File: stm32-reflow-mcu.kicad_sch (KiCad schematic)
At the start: 34 parts, among them J1 TC2030, J10 63824-1, J11 63824-1, J12 63824-1, J2 Conn_01x04_Male, J3 Conn_01x03_Male, J4 Screw_Terminal_01x02, J5 Screw_Terminal_01x02, J7 63824-1, J8 63824-1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

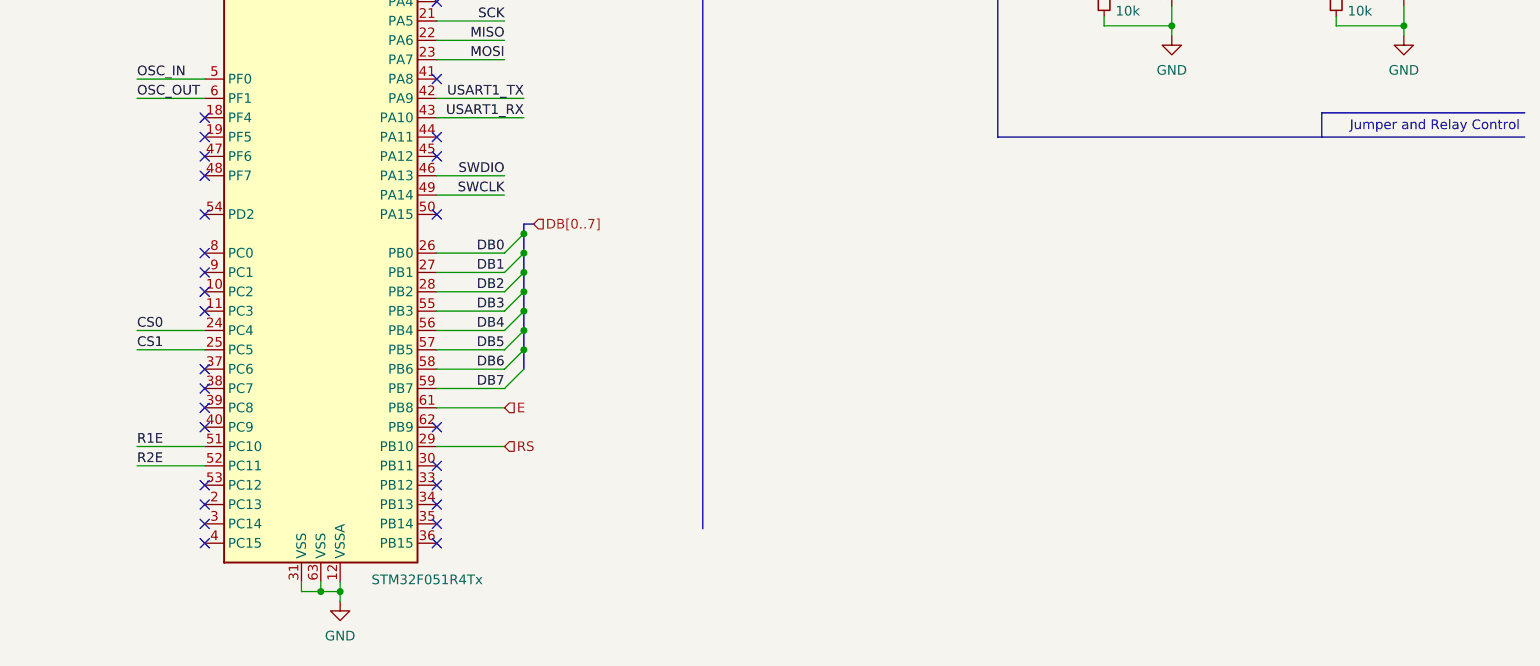
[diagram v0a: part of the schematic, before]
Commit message: added encoder interface
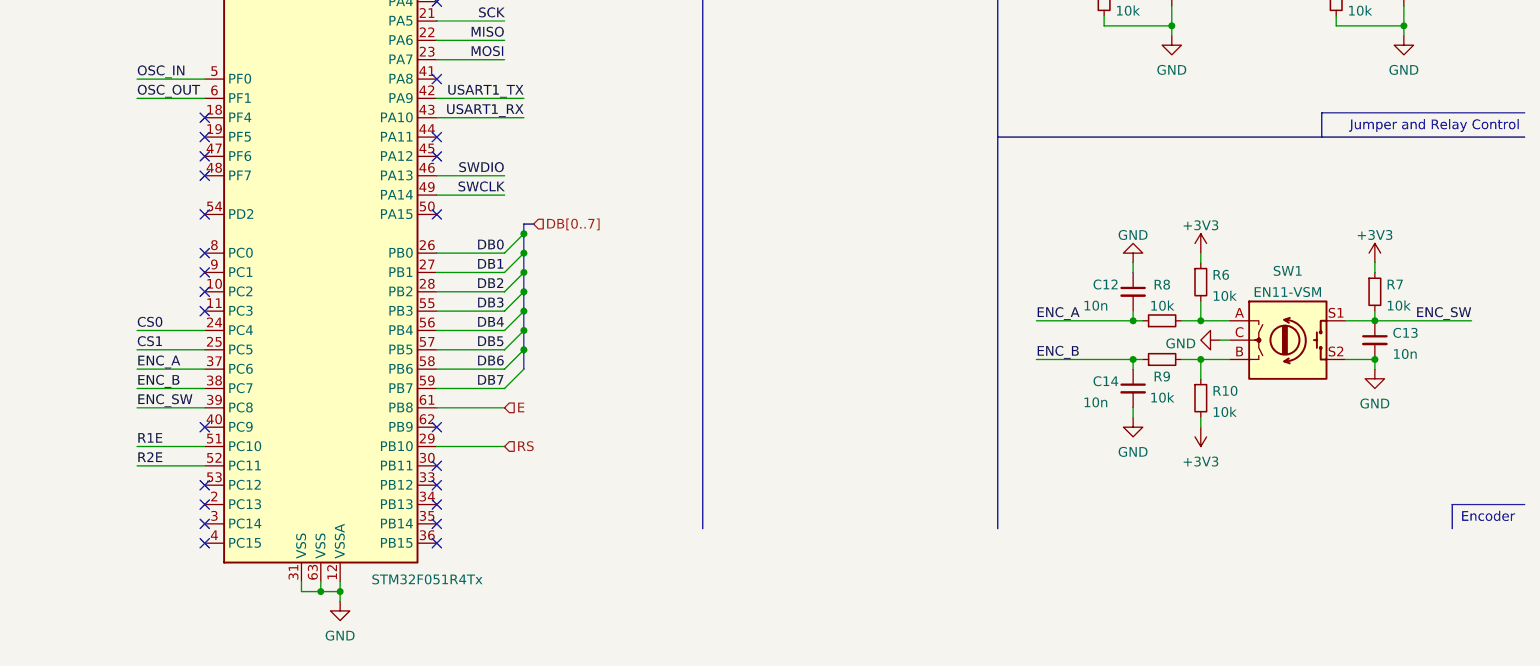
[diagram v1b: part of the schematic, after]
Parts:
- added C12, C13, C14: 10n, Capacitor_SMD:C_0603_1608Metric, symbol Device:C_Small
- added R10, R6, R7, R8, R9: 10k, Resistor_SMD:R_0603_1608Metric, symbol Device:R_Small
- added SW1: EN11-VSM, Personal:EN11-VSM1AF20, symbol Device:Rotary_Encoder_Switch
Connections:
- net +3V3: now also R10.2, R6.1, R7.1
- net GND: now also C12.1, C13.2, C14.2, SW1.C, SW1.S2
- net ENC_A: now reaches U1.37 (PC6)
- net ENC_A: now also C12.2, R8.1
- net ENC_B: now reaches U1.38 (PC7)
- net ENC_B: now also C14.1, R9.1
- net ENC_SW: now reaches U1.39 (PC8)
- net ENC_SW: now also C13.1, R7.2, SW1.S1
- new net: R6.2, R8.2, SW1.A
- new net: R10.1, R9.2, SW1.B
- no-connect marks 33 -> 30
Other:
- note added: "Encoder"

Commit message: added revision label, finalized for fabrication
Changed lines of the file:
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@@
   (title_block
     (title "STM32 Reflow Controller")
-    (date "2021-11-26")
+    (date "2021-11-29")
+    (rev "07684a7")
     (company "de Byl Technologies, LLC")
   )

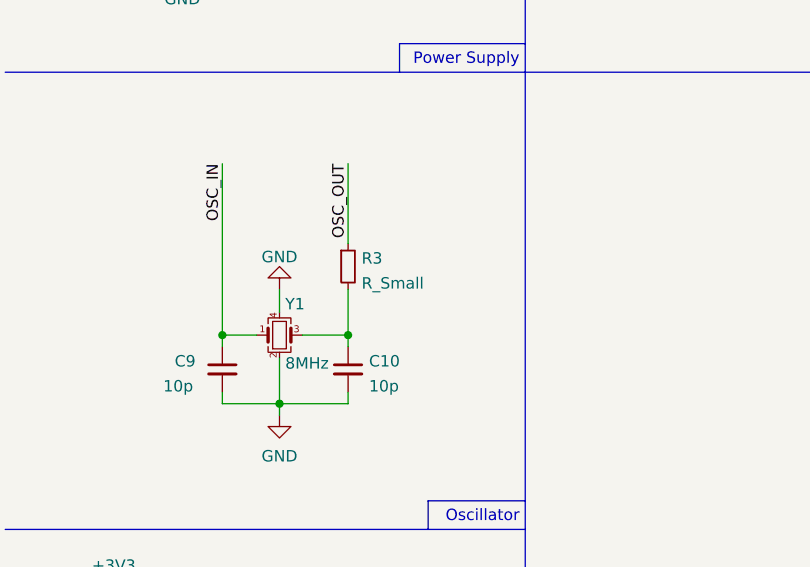
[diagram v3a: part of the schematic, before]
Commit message: updated bom to reflect non-backordered parts
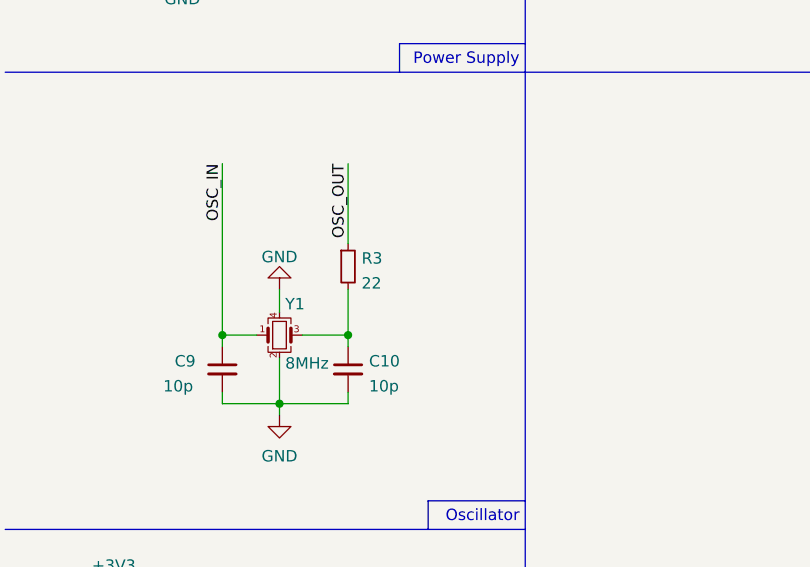
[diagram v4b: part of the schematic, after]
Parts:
- C1, C12, C13, C14, C2, C3, C4, C7, C8: DigiKey Part # (none) -> 732-8007-2-ND
- C10, C11, C5, C6, C9: DigiKey Part # (none) -> 732-7760-2-ND
- J1: now left out of the parts list
- J10, J11, J12, J7, J8, J9: DigiKey Part # (none) -> A29938CT-ND
- J4, J5: DigiKey Part # (none) -> ED10561-ND
- Q12, Q2: DigiKey Part # (none) -> 1727-8642-1-ND
- R1, R10, R4, R5, R6, R7, R8, R9: DigiKey Part # (none) -> RMCF0603JT10K0TR-ND
- R3: value R_Small -> 22; DigiKey Part # (none) -> CR0603-JW-220ELFTR-ND
- SW1: DigiKey Part # (none) -> 987-1192-ND
- U4: DigiKey Part # (none) -> 497-3455-2-ND
- Y1: DigiKey Part # (none) -> 1923-LFXTAL061627REELCT-ND
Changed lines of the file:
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@@
       (effects (font (size 1.27 1.27)) (justify left))
     )
-    (property "Value" "R_Small" (id 1) (at 51.6636 74.2566 0)
+    (property "Value" "22" (id 1) (at 51.6636 74.2566 0)
       (effects (font (size 1.27 1.27)) (justify left))
     )
@@
       (effects (font (size 1.27 1.27)) hide)
     )
+    (property "DigiKey Part #" "CR0603-JW-220ELFTR-ND" (id 4) (at 50.165 72.39 0)
+      (effects (font (size 1.27 1.27)) hide)
+    )
     (pin "1")
     (pin "2")
@@
       (effects (font (size 1.27 1.27)) hide)
     )
+    (property "DigiKey Part #" "RMCF0603JT10K0TR-ND" (id 4) (at 146.05 31.75 0)
+      (effects (font (size 1.27 1.27)) hide)
+    )
     (pin "1")
     (pin "2")
@@
     )
     (property "Datasheet" "~" (id 3) (at 229.87 95.885 0)
+      (effects (font (size 1.27 1.27)) hide)
+    )
+    (property "DigiKey Part #" "RMCF0603JT10K0TR-ND" (id 4) (at 229.87 95.885 0)
       (effects (font (size 1.27 1.27)) hide)
     )
@@
     )
     (property "Datasheet" "~" (id 3) (at 237.49 138.43 0)
+      (effects (font (size 1.27 1.27)) hide)
+    )
+    (property "DigiKey Part #" "RMCF0603JT10K0TR-ND" (id 4) (at 237.49 138.43 0)
       (effects (font (size 1.27 1.27)) hide)
     )
@@
       (effects (font (size 1.27 1.27)) hide)
     )
+    (property "DigiKey Part #" "RMCF0603JT10K0TR-ND" (id 4) (at 237.49 143.51 0)
+      (effects (font (size 1.27 1.27)) hide)
+    )
     (pin "1")
     (pin "2")
@@
       (effects (font (size 1.27 1.27)) hide)
     )
+    (property "DigiKey Part #" "RMCF0603JT10K0TR-ND" (id 4) (at 242.57 133.35 0)
+      (effects (font (size 1.27 1.27)) hide)
+    )
     (pin "1")
     (pin "2")
@@
       (effects (font (size 1.27 1.27)) hide)
     )
+    (property "DigiKey Part #" "RMCF0603JT10K0TR-ND" (id 4) (at 242.57 148.59 0)
+      (effects (font (size 1.27 1.27)) hide)
+    )
     (pin "1")
     (pin "2")
@@
       (effects (font (size 1.27 1.27)) hide)
     )
+    (property "DigiKey Part #" "RMCF0603JT10K0TR-ND" (id 4) (at 260.35 95.885 0)
+      (effects (font (size 1.27 1.27)) hide)
+    )
     (pin "1")
     (pin "2")
@@
       (effects (font (size 1.27 1.27)) hide)
     )
+    (property "DigiKey Part #" "RMCF0603JT10K0TR-ND" (id 4) (at 265.43 134.62 0)
+      (effects (font (size 1.27 1.27)) hide)
+    )
     (pin "1")
     (pin "2")
@@
       (effects (font (size 1.27 1.27)) hide)
     )
+    (property "DigiKey Part #" "732-8007-2-ND" (id 4) (at 24.13 113.03 0)
+      (effects (font (size 1.27 1.27)) hide)
+    )
     (pin "1")
     (pin "2")
@@
       (effects (font (size 1.27 1.27)) hide)
     )
+    (property "DigiKey Part #" "732-8007-2-ND" (id 4) (at 24.13 157.48 0)
+      (effects (font (size 1.27 1.27)) hide)
+    )
     (pin "1")
     (pin "2")
@@
     )
     (property "Datasheet" "~" (id 3) (at 31.75 30.48 0)
+      (effects (font (size 1.27 1.27)) hide)
+    )
+    (property "DigiKey Part #" "732-7760-2-ND" (id 4) (at 31.75 30.48 0)
       (effects (font (size 1.27 1.27)) hide)
     )
@@
       (effects (font (size 1.27 1.27)) hide)
     )
+    (property "DigiKey Part #" "732-7760-2-ND" (id 4) (at 36.195 83.82 0)
+      (effects (font (size 1.27 1.27)) hide)
+    )
     (pin "1")
     (pin "2")
@@
       (effects (font (size 1.27 1.27)) hide)
     )
+    (property "DigiKey Part #" "732-7760-2-ND" (id 4) (at 50.165 83.82 0)
+      (effects (font (size 1.27 1.27)) hide)
+    )
     (pin "1")
     (pin "2")
@@
       (effects (font (size 1.27 1.27)) hide)
     )
+    (property "DigiKey Part #" "732-8007-2-ND" (id 4) (at 74.295 30.48 0)
+      (effects (font (size 1.27 1.27)) hide)
+    )
     (pin "1")
     (pin "2")
@@
       (effects (font (size 1.27 1.27)) hide)
     )
+    (property "DigiKey Part #" "732-8007-2-ND" (id 4) (at 81.915 30.48 0)
+      (effects (font (size 1.27 1.27)) hide)
+    )
     (pin "1")
     (pin "2")
@@
       (effects (font (size 1.27 1.27)) hide)
     )
+    (property "DigiKey Part #" "732-8007-2-ND" (id 4) (at 89.535 30.48 0)
+      (effects (font (size 1.27 1.27)) hide)
+    )
     (pin "1")
     (pin "2")
@@
       (effects (font (size 1.27 1.27)) hide)
     )
+    (property "DigiKey Part #" "732-8007-2-ND" (id 4) (at 97.155 30.48 0)
+      (effects (font (size 1.27 1.27)) hide)
+    )
     (pin "1")
     (pin "2")
@@
       (effects (font (size 1.27 1.27)) hide)
     )
+    (property "DigiKey Part #" "732-7760-2-ND" (id 4) (at 104.775 30.48 0)
+      (effects (font (size 1.27 1.27)) hide)
+    )
     (pin "1")
     (pin "2")
@@
     )
     (property "Datasheet" "~" (id 3) (at 117.475 30.48 0)
+      (effects (font (size 1.27 1.27)) hide)
+    )
+    (property "DigiKey Part #" "732-7760-2-ND" (id 4) (at 117.475 30.48 0)
       (effects (font (size 1.27 1.27)) hide)
     )
@@
       (effects (font (size 1.27 1.27)) hide)
     )
+    (property "DigiKey Part #" "732-8007-2-ND" (id 4) (at 233.68 134.62 0)
+      (effects (font (size 1.27 1.27)) hide)
+    )
     (pin "1")
     (pin "2")
@@
       (effects (font (size 1.27 1.27)) hide)
     )
+    (property "DigiKey Part #" "732-8007-2-ND" (id 4) (at 233.68 147.32 0)
+      (effects (font (size 1.27 1.27)) hide)
+    )
     (pin "1")
     (pin "2")
@@
     )
     (property "Datasheet" "~" (id 3) (at 265.43 140.97 0)
+      (effects (font (size 1.27 1.27)) hide)
+    )
+    (property "DigiKey Part #" "732-8007-2-ND" (id 4) (at 265.43 140.97 0)
       (effects (font (size 1.27 1.27)) hide)
     )
@@
       (effects (font (size 1.27 1.27)) hide)
     )
+    (property "DigiKey Part #" "1923-LFXTAL061627REELCT-ND" (id 4) (at 42.545 80.01 0)
+      (effects (font (size 1.27 1.27)) hide)
+    )
     (pin "1")
     (pin "2")
@@
       (effects (font (size 1.27 1.27)) hide)
     )
+    (property "DigiKey Part #" "ED10561-ND" (id 4) (at 24.13 127 0)
+      (effects (font (size 1.27 1.27)) hide)
+    )
     (pin "1")
     (pin "2")
@@
     )
     (property "Datasheet" "~" (id 3) (at 24.13 171.45 0)
+      (effects (font (size 1.27 1.27)) hide)
+    )
+    (property "DigiKey Part #" "ED10561-ND" (id 4) (at 24.13 171.45 0)
       (effects (font (size 1.27 1.27)) hide)
     )
@@
       (effects (font (size 1.27 1.27)) (justify left bottom) hide)
     )
+    (property "DigiKey Part #" "A29938CT-ND" (id 6) (at 24.13 25.4 0)
+      (effects (font (size 1.27 1.27)) hide)
+    )
     (pin "1")
     (pin "2")
@@
       (effects (font (size 1.27 1.27)) (justify left bottom) hide)
     )
+    (property "DigiKey Part #" "A29938CT-ND" (id 6) (at 24.13 35.56 0)
+      (effects (font (size 1.27 1.27)) hide)
+    )
     (pin "1")
     (pin "2")
@@
       (effects (font (size 1.27 1.27)) (justify left bottom) hide)
     )
+    (property "DigiKey Part #" "A29938CT-ND" (id 6) (at 231.14 74.295 0)
+      (effects (font (size 1.27 1.27)) hide)
+    )
     (pin "1")
     (pin "2")
@@
       (effects (font (size 1.27 1.27)) (justify left bottom) hide)
     )
+    (property "DigiKey Part #" "A29938CT-ND" (id 6) (at 231.14 84.455 0)
+      (effects (font (size 1.27 1.27)) hide)
+    )
     (pin "1")
     (pin "2")
@@
       (effects (font (size 1.27 1.27)) (justify left bottom) hide)
     )
+    (property "DigiKey Part #" "A29938CT-ND" (id 6) (at 261.62 74.295 0)
+      (effects (font (size 1.27 1.27)) hide)
+    )
     (pin "1")
     (pin "2")
@@
       (effects (font (size 1.27 1.27)) (justify left bottom) hide)
     )
+    (property "DigiKey Part #" "A29938CT-ND" (id 6) (at 261.62 84.455 0)
+      (effects (font (size 1.27 1.27)) hide)
+    )
     (pin "1")
     (pin "2")
@@
       (effects (font (size 1.27 1.27)) (justify left) hide)
     )
+    (property "DigiKey Part #" "1727-8642-1-ND" (id 4) (at 236.22 92.075 0)
+      (effects (font (size 1.27 1.27)) hide)
+    )
     (pin "1")
     (pin "2")
@@
     (property "Datasheet" "https://www.fairchildsemi.com/datasheets/2N/2N7002.pdf" (id 3) (at 266.7 92.075 0)
       (effects (font (size 1.27 1.27)) (justify left) hide)
+    )
+    (property "DigiKey Part #" "1727-8642-1-ND" (id 4) (at 266.7 92.075 0)
+      (effects (font (size 1.27 1.27)) hide)
     )
     (pin "1")
@@
       (effects (font (size 1.27 1.27)) hide)
     )
+    (property "DigiKey Part #" "497-3455-2-ND" (id 4) (at 54.61 27.94 0)
+      (effects (font (size 1.27 1.27)) hide)
+    )
     (pin "1")
     (pin "2")
@@
     )
     (property "Datasheet" "~" (id 3) (at 254 134.366 0)
+      (effects (font (size 1.27 1.27)) hide)
+    )
+    (property "DigiKey Part #" "987-1192-ND" (id 4) (at 254 140.97 0)
       (effects (font (size 1.27 1.27)) hide)
     )
@@
   )
   (symbol (lib_id "Personal:TC2030") (at 250.825 28.575 0) (unit 1)
-    (in_bom yes) (on_board yes)
+    (in_bom no) (on_board yes)
     (property "Reference" "J1" (id 0) (at 250.825 20.8493 0))
     (property "Value" "TC2030" (id 1) (at 250.825 36.3244 0))

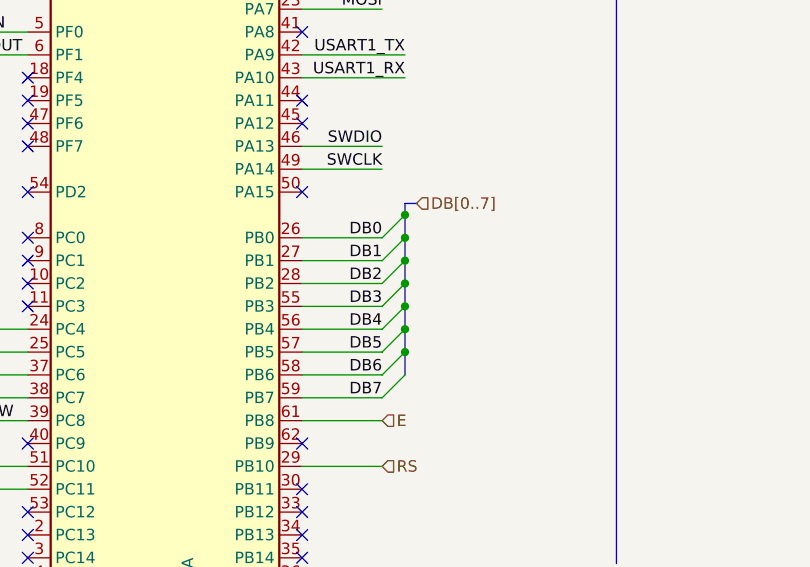
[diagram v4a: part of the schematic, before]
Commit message: updated board for proper kicad6.0 compati
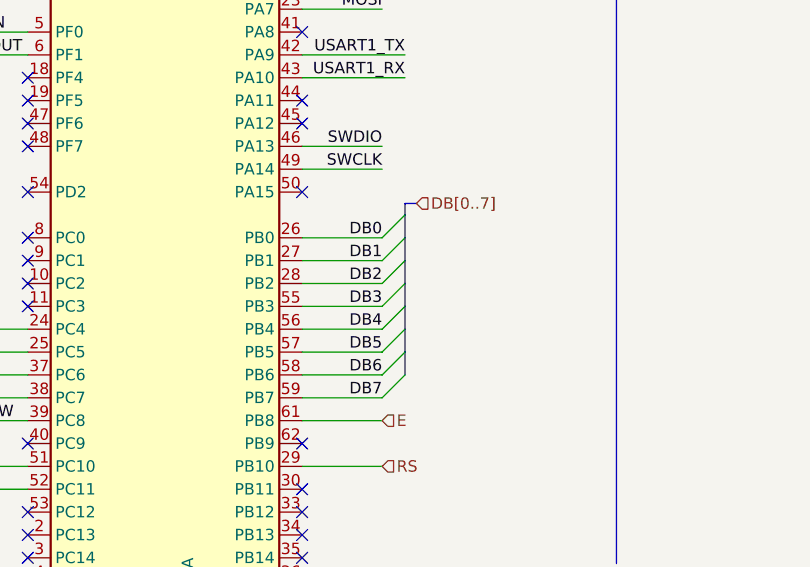
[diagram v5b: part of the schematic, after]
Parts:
- U4: DigiKey Part # 497-3455-2-ND -> (none)
